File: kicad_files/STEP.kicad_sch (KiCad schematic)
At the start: 8 parts

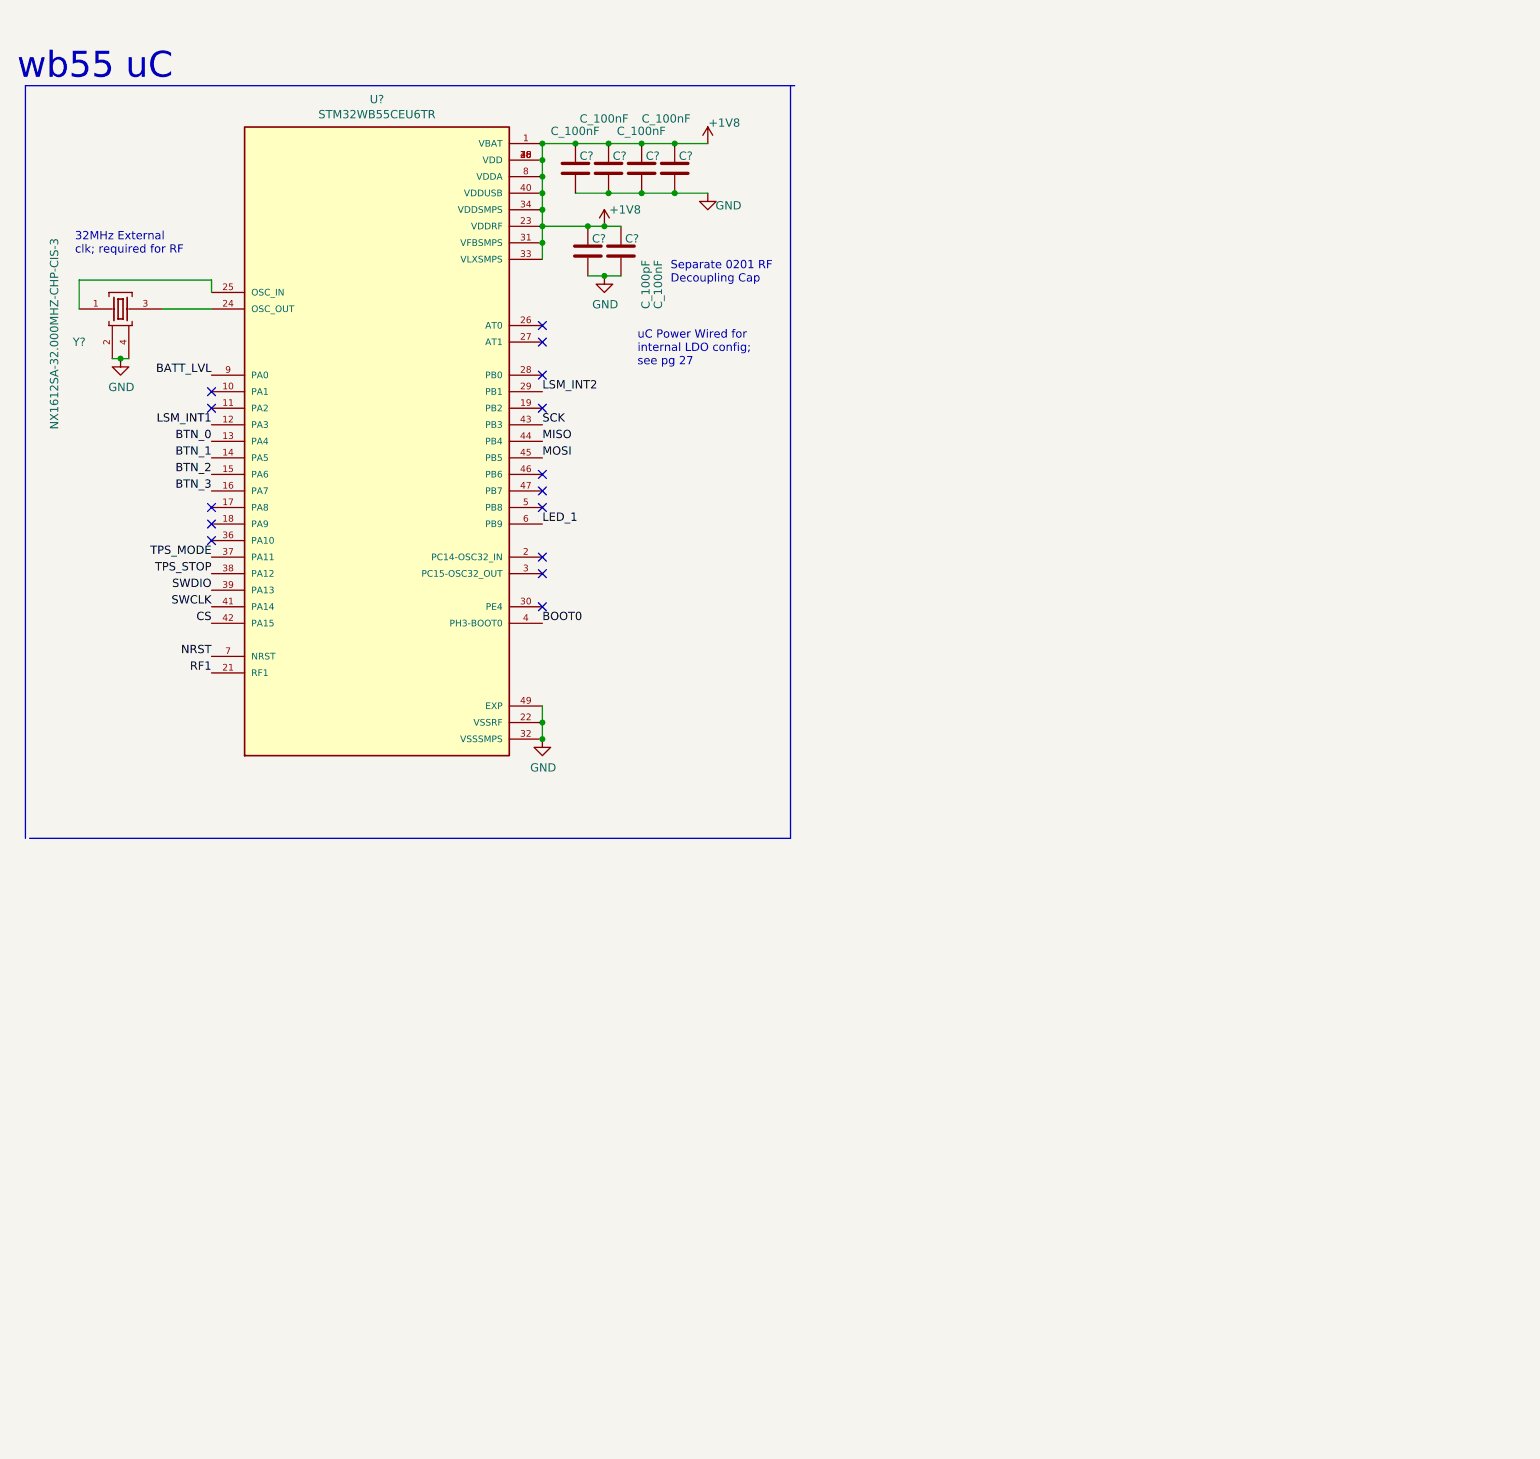
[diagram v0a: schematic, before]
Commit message: Added previous modules to schematic and edited MCU pinouts for 2023 project
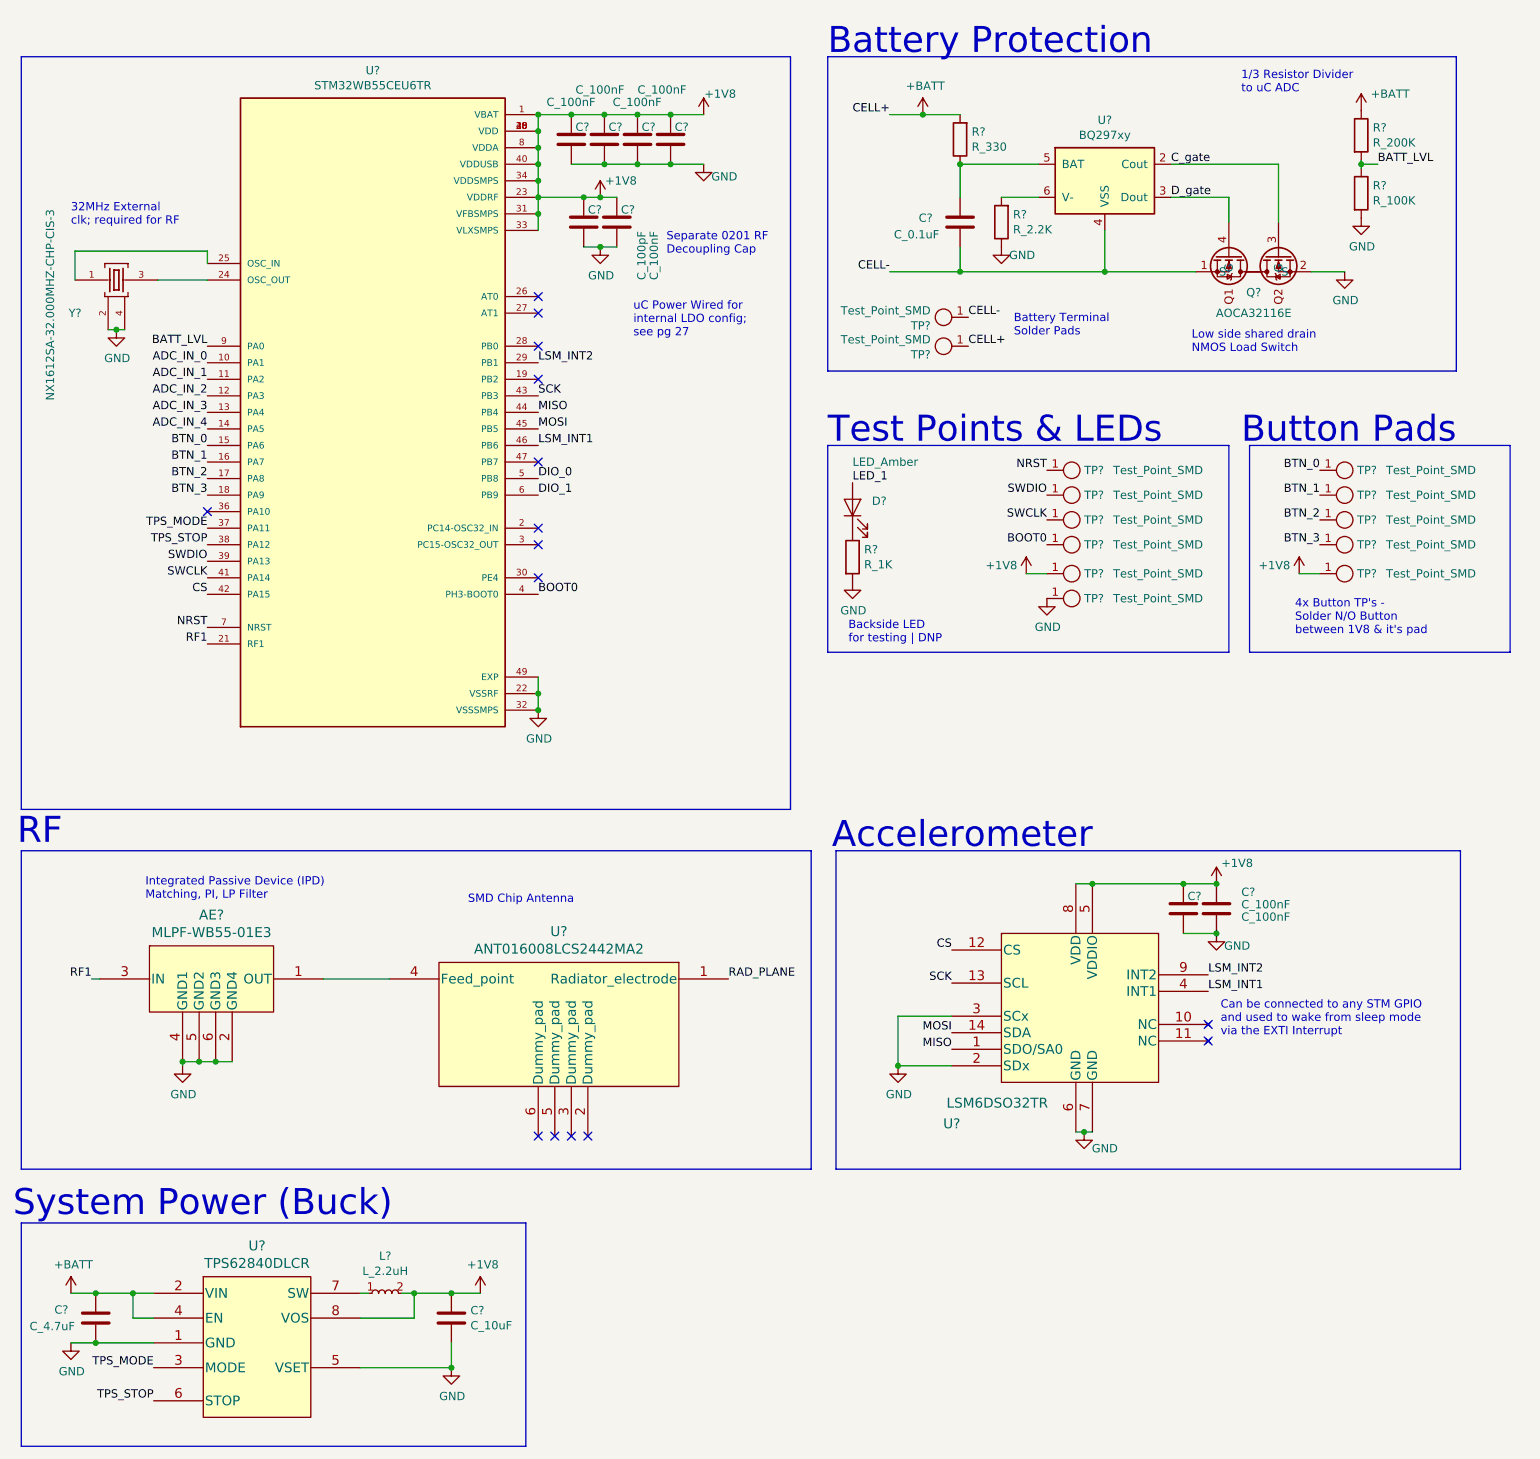
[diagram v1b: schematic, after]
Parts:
- removed C? (x4): C_100nF, Capacitor_SMD:C_0402_1005Metric, symbol ring-rescue:C_100nF-step
- removed C?: C_100pF, Capacitor_SMD:C_0201_0603Metric, symbol ring-rescue:C_100pF-step
- removed C?: C_100nF, Capacitor_SMD:C_0201_0603Metric, symbol ring-rescue:C_100nF-step
- removed U?: STM32WB55CEU6TR, step-footprints:QFN50P700X700X60-49N, symbol ring-rescue:STM32WB55CEU6TR-step
- removed Y?: NX1612SA-32.000MHZ-CHP-CIS-3, step-footprints:OSCSC105P160X120X35-4N, symbol ring-rescue:NX1612SA-32.000MHZ-CHP-CIS-3-step
- added AE?: MLPF-WB55-01E3, step-footprints:MLPF-WB55-01E3, symbol ring-rescue:MLPF-WB55-01E3-step
- added C? (x6): C_100nF, Capacitor_SMD:C_0402_1005Metric, symbol ring-rescue:C_100nF-step
- added C?: C_10uF, Capacitor_SMD:C_0402_1005Metric, symbol ring-rescue:C_10uF-step
- added C?: C_100nF, Capacitor_SMD:C_0201_0603Metric, symbol ring-rescue:C_100nF-step
- added C?: C_100pF, Capacitor_SMD:C_0201_0603Metric, symbol ring-rescue:C_100pF-step
- added C?: C_0.1uF, Capacitor_SMD:C_0402_1005Metric, symbol ring-rescue:C_0.1uF-step
- added C?: C_4.7uF, Capacitor_SMD:C_0402_1005Metric, symbol ring-rescue:C_4.7uF-step
- added D?: LED_Amber, LED_SMD:LED_0402_1005Metric, symbol ring-rescue:LED_0805_Amber-step
- added L?: L_2.2uH, Inductor_SMD:L_0805_2012Metric_Pad1.05x1.20mm_HandSolder, symbol ring-rescue:L_2.2uH-step
- added Q?: AOCA32116E, step-footprints:AOCA32116E, symbol ring-rescue:AOCA32116E-step
- added R?: R_100K, Resistor_SMD:R_0402_1005Metric, symbol ring-rescue:R_100K-step
- added R?: R_2.2K, Resistor_SMD:R_0402_1005Metric, symbol ring-rescue:R_2.2K-step
- added R?: R_1K, Resistor_SMD:R_0402_1005Metric, symbol ring-rescue:R_1K-step
- added R?: R_200K, Resistor_SMD:R_0402_1005Metric, symbol ring-rescue:R_200K-step
- added R?: R_330, Resistor_SMD:R_0402_1005Metric, symbol ring-rescue:R_330-step
- added TP? (x2): Test_Point_SMD, TestPoint:TestPoint_Pad_1.5x1.5mm, symbol ring-rescue:Test_Point_SMD-step
- added TP? (x11): Test_Point_SMD, TestPoint:TestPoint_Pad_1.0x1.0mm, symbol ring-rescue:Test_Point_SMD-step
- added U?: ANT016008LCS2442MA2, step-footprints:ANT016008LCS2442MA2, symbol ring-rescue:ANT016008LCS2442MA2-step
- added U?: TPS62840DLCR, step-footprints:TPS62840DLCR, symbol ring-rescue:TPS62840DLCR-step
- added U?: STM32WB55CEU6TR, step-footprints:QFN50P700X700X60-49N, symbol ring-rescue:STM32WB55CEU6TR-step
- added U?: LSM6DSO32TR, step-footprints:LSM6DSO32TR, symbol ring-rescue:LSM6DSO32TR-step
- added U?: BQ297xy, Package_SON:WSON-6_1.5x1.5mm_P0.5mm, symbol Battery_Management:BQ297xy
- added Y?: NX1612SA-32.000MHZ-CHP-CIS-3, step-footprints:OSCSC105P160X120X35-4N, symbol ring-rescue:NX1612SA-32.000MHZ-CHP-CIS-3-step
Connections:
- net +1V8: now also C?.1, C?.1, C?.1, C?.1, C?.1, C?.1, C?.1, C?.1, C?.1, L?.2, TP?.1, TP?.1, U?.1 (VBAT), U?.20 (VDD), U?.23 (VDDRF), U?.31 (VFBSMPS), U?.33 (VLXSMPS), U?.34 (VDDSMPS), U?.35 (VDD), U?.40 (VDDUSB), U?.48 (VDD), U?.5 (VDDIO), U?.8 (VDD), U?.8 (VDDA), U?.8 (VOS)
- net BATT_LVL: now also R?.1, R?.2, U?.9 (PA0)
- net BOOT0: now also TP?.1, U?.4 (PH3-BOOT0)
- net BTN_0: now also TP?.1, U?.15 (PA6)
- net BTN_1: now also TP?.1, U?.16 (PA7)
- net BTN_2: now also TP?.1, U?.17 (PA8)
- net BTN_3: now also TP?.1, U?.18 (PA9)
- net CS: now also U?.12 (CS), U?.42 (PA15)
- net GND: now also AE?.2 (GND4), AE?.4 (GND1), AE?.5 (GND2), AE?.6 (GND3), C?.2, C?.2, C?.2, C?.2, C?.2, C?.2, C?.2, C?.2, C?.2, C?.2, Q?.2 (S), R?.1, R?.2, R?.2, TP?.1, U?.1 (GND), U?.2 (SDx), U?.22 (VSSRF), U?.3 (SCx), U?.32 (VSSSMPS), U?.49 (EXP), U?.5 (VSET), U?.6 (GND), U?.7 (GND), Y?.2, Y?.4
- net LED_1: now also D?.2 (A)
- net LSM_INT1: now also U?.4 (INT1), U?.46 (PB6)
- net LSM_INT2: now also U?.29 (PB1), U?.9 (INT2)
- net MISO: now also U?.1 (SDO/SA0), U?.44 (PB4)
- net MOSI: now also U?.14 (SDA), U?.45 (PB5)
- net NRST: now also TP?.1, U?.7 (NRST)
- net RF1: now also AE?.3 (IN), U?.21 (RF1)
- net SCK: now also U?.13 (SCL), U?.43 (PB3)
- net SWCLK: now also TP?.1, U?.41 (PA14)
- net SWDIO: now also TP?.1, U?.39 (PA13)
- net TPS_MODE: now also U?.3 (MODE), U?.37 (PA11)
- net TPS_STOP: now also U?.38 (PA12), U?.6 (STOP)
- new net: AE?.1 (OUT), U?.4 (Feed_point)
- new net: L?.1, U?.7 (SW)
- new net: U?.24 (OSC_OUT), Y?.3
- new net: U?.25 (OSC_IN), Y?.1
- new net: C?.1, R?.1, U?.5 (BAT)
- new net: R?.2, U?.6 (V-)
- new net: D?.1 (K), R?.1
- new net +BATT: C?.1, R?.1, R?.2, TP?.1, U?.2 (VIN), U?.4 (EN)
- new net ADC_IN_0: U?.10 (PA1)
- new net ADC_IN_1: U?.11 (PA2)
- new net ADC_IN_2: U?.12 (PA3)
- new net ADC_IN_3: U?.13 (PA4)
- new net ADC_IN_4: U?.14 (PA5)
- new net CELL-: C?.2, Q?.1 (S), TP?.1, U?.4 (VSS)
- new net C_gate: Q?.3 (G), U?.2 (Cout)
- new net DIO_0: U?.5 (PB8)
- new net DIO_1: U?.6 (PB9)
- new net D_gate: Q?.4 (G), U?.3 (Dout)
- new net RAD_PLANE: U?.1 (Radiator_electrode)
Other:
- note added: "1/3 Resistor Divider to uC ADC"
- note added: "4x Button TP's - Solder N/O Button between 1V8 & it's pad"
- note added: "Accelerometer"
- note added: "Backside LED for testing | DNP"
- note added: "Battery Protection"
- note added: "Battery Terminal Solder Pads"
- note added: "Button Pads"
- note added: "Can be connected to any STM GPIO and used to wake from sleep mode via the EXTI Interrupt"
- note added: "Integrated Passive Device (IPD) Matching, PI, LP Filter"
- note added: "Low side shared drain NMOS Load Switch"
- note added: "RF"
- note added: "SMD Chip Antenna"
- note added: "System Power (Buck)"
- note added: "Test Points & LEDs"
- note removed: "wb55 uC"

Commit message: new buck, fixed mc pinout, improvements from v0 ring, haptics, connectors and ADCs
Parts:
- removed C?: C_10uF, Capacitor_SMD:C_0402_1005Metric, symbol ring-rescue:C_10uF-step
- removed C?: C_4.7uF, Capacitor_SMD:C_0402_1005Metric, symbol ring-rescue:C_4.7uF-step
- removed L?: L_2.2uH, Inductor_SMD:L_0805_2012Metric_Pad1.05x1.20mm_HandSolder, symbol ring-rescue:L_2.2uH-step
- removed U?: TPS62840DLCR, step-footprints:TPS62840DLCR, symbol ring-rescue:TPS62840DLCR-step
- added C1: C_4.7uF, Capacitor_SMD:C_0402_1005Metric, symbol ring-rescue:C_4.7uF-step
- added C5: C_10uF, Capacitor_SMD:C_0402_1005Metric, symbol ring-rescue:C_10uF-step
- added C6, C8: C_100pF, Capacitor_SMD:C_0201_0603Metric, symbol ring-rescue:C_100pF-step
- added C7: C_10nF, Capacitor_SMD:C_0402_1005Metric, symbol ring-rescue:C_0.1uF-step
- added J1: CONN_MAG_01x03, symbol step_symbols_main:CONN_MAG_01x03
- added J2: CONN_MAG_01x04, symbol step_symbols_main:CONN_MAG_01x04
- added J3: CONN_MAG_01x09, symbol step_symbols_main:CONN_MAG_01x09
- added L1: L_2.2uH, Inductor_SMD:L_0805_2012Metric_Pad1.05x1.20mm_HandSolder, symbol ring-rescue:L_2.2uH-step
- added Q2, Q3: SSM3K35CTC, symbol step_symbols_main:SSM3K35CTC
- added R10, R11, R12, R6, R7, R8, R9: R_10K, Resistor_SMD:R_0402_1005Metric, symbol ring-rescue:R_200K-step
- added TP14, TP15, TP16, TP17, TP18, TP19, TP20: Test_Point_SMD, TestPoint:TestPoint_Pad_1.0x1.0mm, symbol ring-rescue:Test_Point_SMD-step
- added U3: LM3671TL-1V8/NOPB, symbol step_symbols_main:LM3671TL-1V8/NOPB
- added U6: PKMCS0909E4000-R1, symbol step_symbols_main:PKMCS0909E4000-R1
- gave numbers to parts that had none: 35
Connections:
- net ADC_IN_4 is gone; now on net BTN_0: U4.14 (PA5)
- net +1V8: now also C5.1, J1.2, L1.2, R6.2, R8.2, U3.C3 (FB)
- net +BATT: now also C1.1, TP19.1, U3.A1 (VIN), U3.C1 (EN), U6.1
- net ADC_IN_0: now also J3.6, TP15.1
- net ADC_IN_1: now also J3.7, TP16.1
- net ADC_IN_2: now also J3.8, R8.1, R9.2, TP17.1
- net ADC_IN_3: now also J3.9, R6.1, R7.2, TP18.1
- net BOOT0: now also J2.4, R10.2
- net BTN_0: now also J3.1; no longer U4.15 (PA6)
- net BTN_1: now also U4.15 (PA6), J3.2; no longer U4.16 (PA7)
- net BTN_2: now also U4.16 (PA7), J3.3; no longer U4.17 (PA8)
- net BTN_3: now also U4.17 (PA8), J3.4; no longer U4.18 (PA9)
- net GND: now also C1.2, C5.2, C6.2, C7.2, C8.2, J1.1, J1.3, Q2.2 (S), Q3.2 (S), R10.1, R11.1, R12.1, R7.1, R9.1, U3.A3 (GND)
- net NRST: now also C7.1, J2.1
- net SWCLK: now also J2.3
- net SWDIO: now also J2.2
- net at U4.24 (OSC_OUT), Y1.3: now also C8.1
- net at U4.25 (OSC_IN), Y1.1: now also C6.1
- net DIO_0 renamed COIN_CELL_LSD
- net COIN_CELL_LSD: now also Q2.1 (G), Q3.1 (G), R11.2, R12.2
- net DIO_1 renamed PIEZO_SMT_LSD
- net TPS_MODE: no longer names the net of U4.37 (PA11)
- net TPS_STOP: no longer names the net of U4.38 (PA12)
- new net: L1.1, U3.B2 (SW)
- new net: Q3.3 (D), U6.2
- new net: Q2.3 (D), TP20.1
- new net BTN_4: J3.5, TP14.1, U4.18 (PA9)
- no-connect marks 15 -> 17
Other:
- note added: "32MHz External clk; required for RF Minimize trace length"
- note added: "5x Button TP's - Solder N/O Button between 1V8 & it's pad"
- note added: "ADC Breakout"
- note added: "ADC Breakouts"
- note added: "Button Breakout"
- note added: "DNP"
- note added: "Fixed output at 1.8V"
- note added: "For Dial/Joystick compatibility || ADC2/ADC3 pins have DNP divider pads"
- note added: "Haptic Feedback"
- note added: "Intentionally 3.xV Vmin = 1.5V"
- note added: "Intentionally 3.xV haptic coin Vmin = 2V"
- note added: "Internal Pull -Down in SW"
- note added: "JTAG Programming - Use in conjunction with Power connector"
- note added: "Magnetic Connectors"
- note added: "Microcontroller"
- note added: "P/N solder points for coin cell"
- note added: "Peripherals - Use in conjunction with Power connector"
- note added: "Power"
- note added: "Separate 0201 RF Decoupling Cap Minimize length to pin 23"
- note removed: "32MHz External clk; required for RF"
- note removed: "4x Button TP's - Solder N/O Button between 1V8 & it's pad"
- note removed: "Button Pads"
- note removed: "Separate 0201 RF Decoupling Cap"
- moved on the sheet: AE1, C10, C11, C12, C13, C14, C2, C3, C4, C9, D1, Q1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

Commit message: added aux buck, fixed haptic circuit nets
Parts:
- removed TP19, TP20: Test_Point_SMD, TestPoint:TestPoint_Pad_1.0x1.0mm, symbol ring-rescue:Test_Point_SMD-step
- added C?: C_4.7uF, Capacitor_SMD:C_0402_1005Metric, symbol ring-rescue:C_4.7uF-step
- added C?: C_10uF, Capacitor_SMD:C_0402_1005Metric, symbol ring-rescue:C_10uF-step
- added L?: L_2.2uH, Inductor_SMD:L_0805_2012Metric_Pad1.05x1.20mm_HandSolder, symbol ring-rescue:L_2.2uH-step
- added R? (x3): R_10k, Resistor_SMD:R_0402_1005Metric, symbol ring-rescue:R_330-step
- added R? (x3): R_X, Resistor_SMD:R_0402_1005Metric, symbol ring-rescue:R_330-step
- added TP? (x2): Test_Point_SMD, TestPoint:TestPoint_Pad_1.0x1.0mm, symbol ring-rescue:Test_Point_SMD-step
- added U?: LM3671TL-1V8/NOPB, symbol step_symbols_main:LM3671TL-1V8/NOPB
- added U?: PKMCS0909E4000-R1, symbol step_symbols_main:PKMCS0909E4000-R1
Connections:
- net +1V8: now also C?.1, L?.2, R?.2
- net +BATT: now also C?.1, R?.2, R?.2, TP?.1, U?.1, U?.A1 (VIN); no longer U3.C1 (EN)
- net GND: now also C?.2, C?.2, R?.1, R?.1, R?.1, U?.A3 (GND)
- net at Q2.3 (D): now also TP?.1, U?.2
- net COIN_CELL_LSD renamed VBATT_BUZZER_LSD
- net VBATT_BUZZER_LSD: no longer Q3.1 (G), R12.2
- net PIEZO_SMT_LSD renamed VAUX_BUZZER_LSD
- net VAUX_BUZZER_LSD: now also Q3.1 (G), R12.2
- new net: R?.1, R?.2, U?.C1 (EN)
- new net: R?.1, R?.2, U3.C1 (EN)
- new net: L?.1, U?.B2 (SW)
- new net: R?.1, R?.2, U?.C3 (FB)
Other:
- note added: "Auxillary Power (Buck)"
- note added: "DNP SMT for solder pads for coin cell"
- note added: "Variable Voltage. Set on AUX buck Vmin = 1.5V"
- note added: "Variable output (DIFFERENT PN from fixed 1.8V)"
- note removed: "Intentionally 3.xV Vmin = 1.5V"
- note removed: "P/N solder points for coin cell"
- moved on the sheet: C1, C3, C4, C5, J1, J2, J3, L1, Q2, Q3, R11, R12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
